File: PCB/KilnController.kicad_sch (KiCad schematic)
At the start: 26 parts, among them J1 12V 3A PS Header, J10 Display Header, J11 Display Button Header, J2 Exhaust Fan Header, J3 Circulation Fan Header, J4 SD Card Module, J5 Exhaust Servo Header, J6 Intake Servo Header, J7 Lumber Zone SHT31 Header, J8 Intake Zone SHT31 Header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

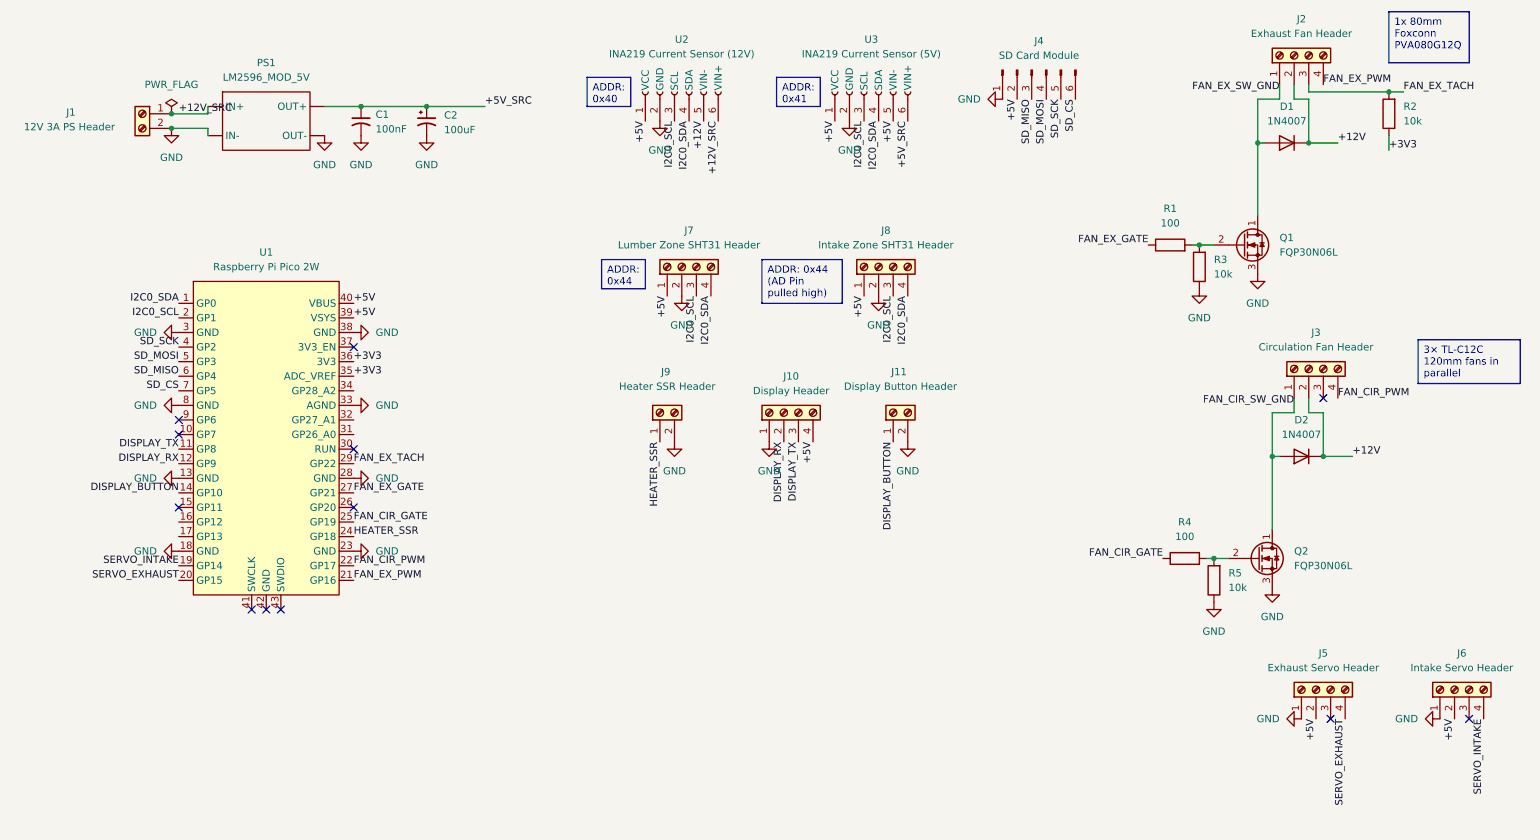
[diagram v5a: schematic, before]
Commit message: Update Display Button GPIO
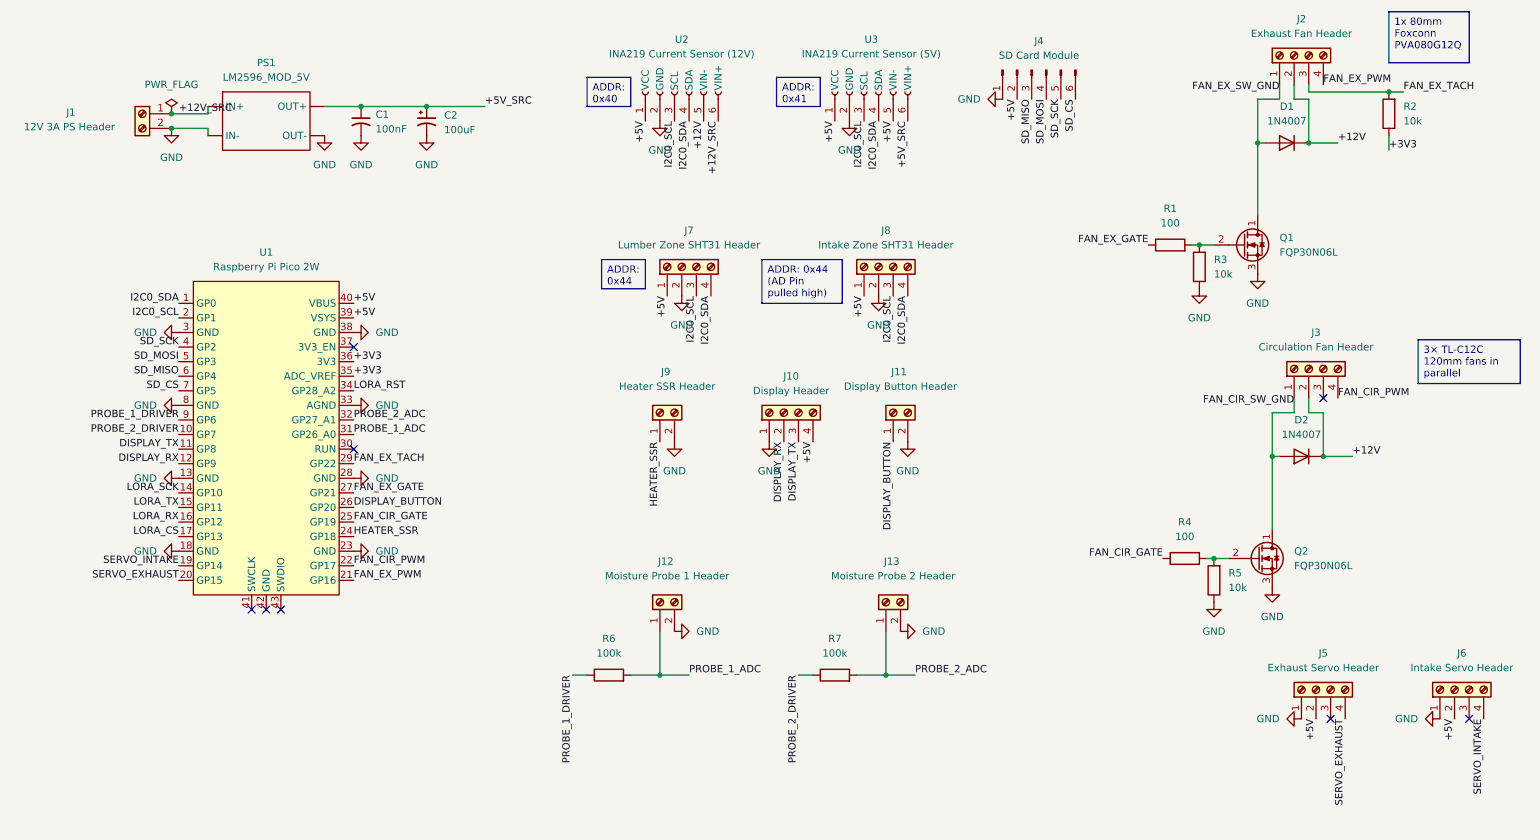
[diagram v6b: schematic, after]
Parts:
- added J12: Moisture Probe 1 Header, TerminalBlock_MetzConnect:TerminalBlock_MetzConnect_Type101_RT01602HBWC_1x02_P5.08mm_Horizontal, symbol Connector:Screw_Terminal_01x02
- added J13: Moisture Probe 2 Header, TerminalBlock_MetzConnect:TerminalBlock_MetzConnect_Type101_RT01602HBWC_1x02_P5.08mm_Horizontal, symbol Connector:Screw_Terminal_01x02
- added R6, R7: 100k, Resistor_THT:R_Axial_DIN0207_L6.3mm_D2.5mm_P10.16mm_Horizontal, symbol Device:R
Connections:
- net DISPLAY_BUTTON: now also U1.26 (GP20); no longer U1.14 (GP10)
- net GND: now also J12.2 (Pin_2), J13.2 (Pin_2)
- net PROBE_2_DRIVER: now reaches U1.10 (GP7)
- net PROBE_2_DRIVER: now also R7.1
- net LORA_TX: now reaches U1.15 (GP11)
- net LORA_RX: now reaches U1.16 (GP12)
- net LORA_CS: now reaches U1.17 (GP13)
- net PROBE_1_ADC: now reaches U1.31 (GP26_A0)
- net PROBE_1_ADC: now also J12.1 (Pin_1), R6.2
- net PROBE_2_ADC: now reaches U1.32 (GP27_A1)
- net PROBE_2_ADC: now also J13.1 (Pin_1), R7.2
- net LORA_RST: now reaches U1.34 (GP28_A2)
- net PROBE_1_DRIVER: now reaches U1.9 (GP6)
- net PROBE_1_DRIVER: now also R6.1
- new net LORA_SCK: U1.14 (GP10)
- no-connect marks 12 -> 8

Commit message: Add LoRa to schematic & layout
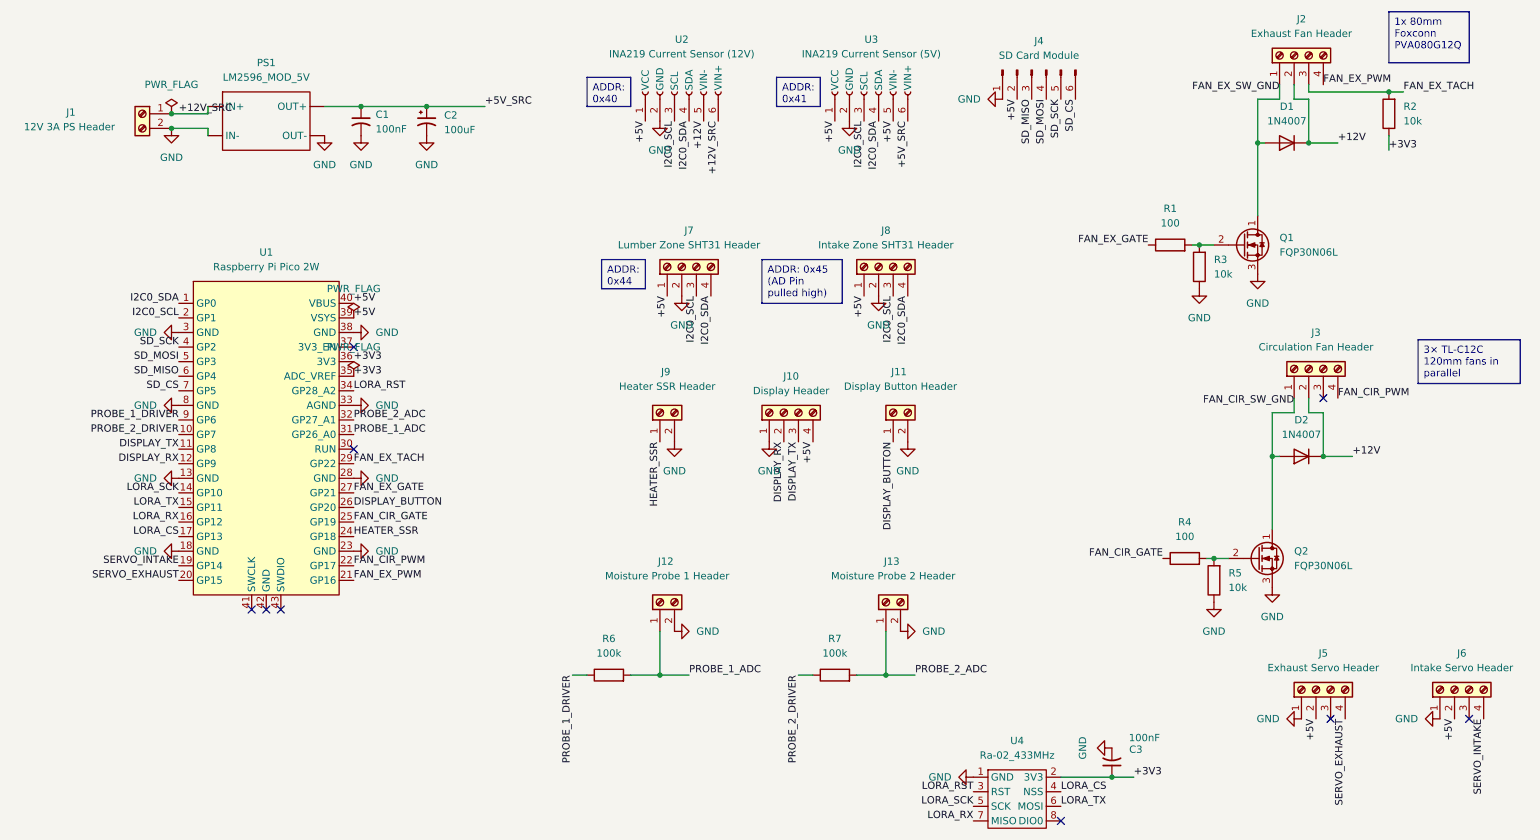
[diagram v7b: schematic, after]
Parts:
- added C3: 100nF, Capacitor_THT:C_Disc_D5.0mm_W2.5mm_P5.00mm, symbol Device:C_Small_US
- added U4: Ra-02_433MHz, KilnFootprintLibrary:LoRa_Module, symbol KilnSymbols:Ra02_LoRa
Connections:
- net +3V3: now also C3.1, U4.2 (3V3)
- net GND: now also C3.2, U4.1 (GND)
- net LORA_CS: now also U4.4 (NSS)
- net LORA_RST: now also U4.3 (RST)
- net LORA_RX: now also U4.7 (MISO)
- net LORA_SCK: now also U4.5 (SCK)
- net LORA_TX: now also U4.6 (MOSI)
- no-connect marks 8 -> 9

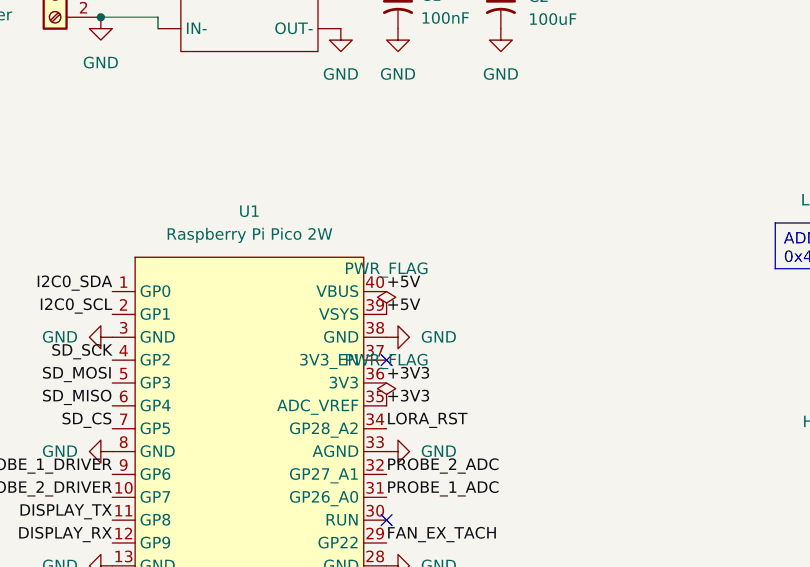
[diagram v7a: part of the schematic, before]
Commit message: Remove VBUS connection
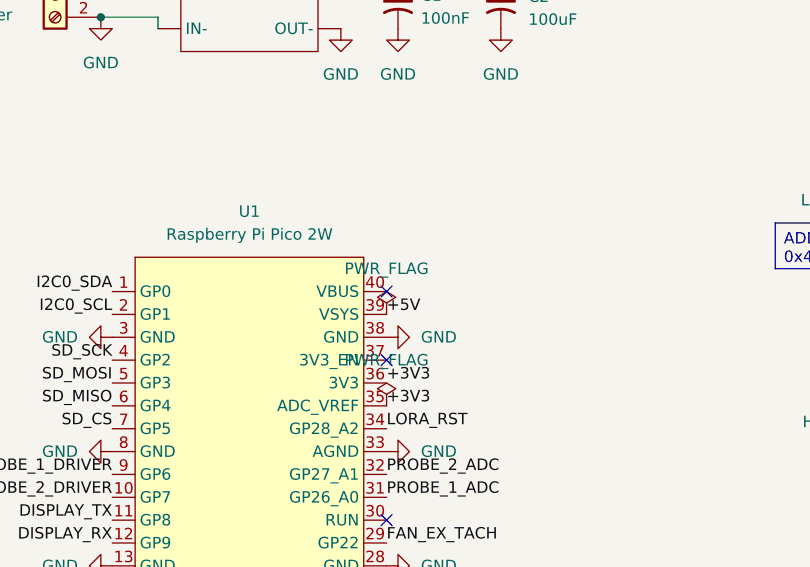
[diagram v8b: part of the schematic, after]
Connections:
- net +5V: no longer U1.40 (VBUS)
- no-connect marks 9 -> 10
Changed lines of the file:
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@@
+	)
+	(no_connect
+		(at 78.74 67.31)
 	)
 	(no_connect
@@
 		(effects
 			(font
-				(size 1.27 1.27)
-			)
-			(justify left bottom)
-		)
-	)
-	(label "+5V"
-		(at 78.74 67.31 0)
-		(effects
-			(font
